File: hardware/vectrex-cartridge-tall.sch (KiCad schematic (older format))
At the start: 15 parts, among them CON1 vectrex-edge-connector, SW1 SW_DIP_x03, U1 AT27C256R-70PU / AT27C512R-70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, U2 DS2431+ TO-92

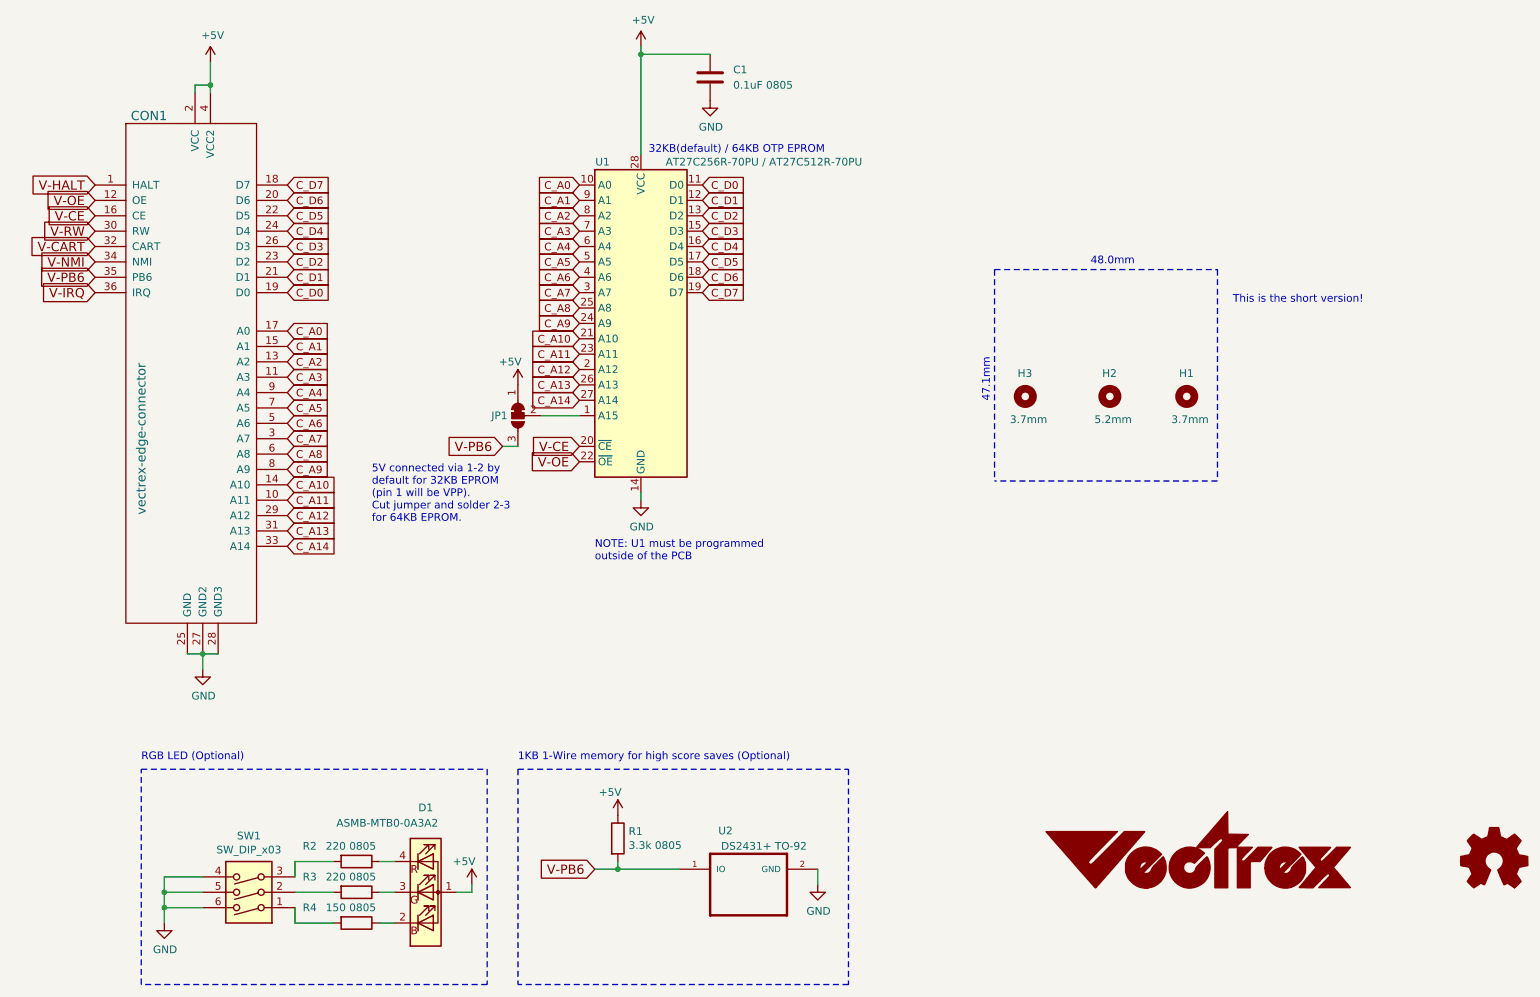
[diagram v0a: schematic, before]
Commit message: Updated DS2431 footprint, and many little tweaks for v1.2
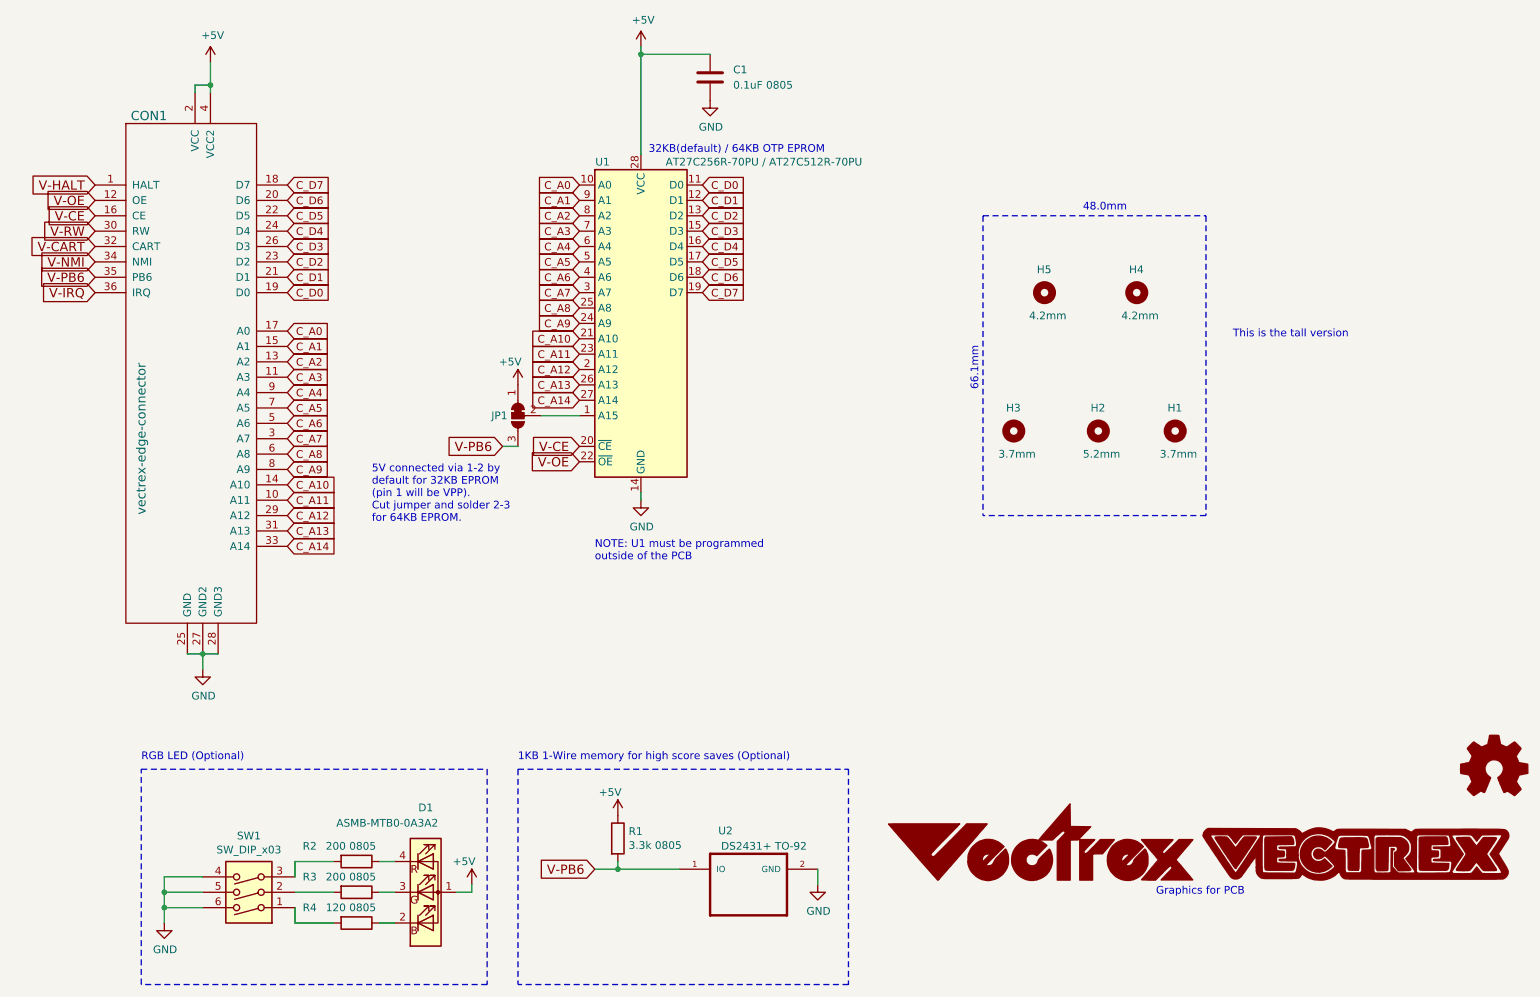
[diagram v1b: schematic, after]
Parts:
- added G3: LOGO, vectrex-cartridge:vectrex-uk-soldermask, symbol vectrex-uk:LOGO
- added H4, H5: 4.2mm, vectrex-cartridge:Mounting_Hole_D4.2mm, symbol Mechanical:MountingHole
- G1: footprint vectrex-cartridge:vectrex-us-soldermask-15mm -> vectrex-cartridge:vectrex-us-soldermask
- R2, R3: value 220 0805 -> 200 0805
- R4: value 150 0805 -> 120 0805
- U2: footprint vectrex-cartridge:TO-92L_HandSolder -> vectrex-cartridge:TO-92_Inline_BW
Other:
- note added: "66.1mm\n"
- note added: "Graphics for PCB"
- note added: "This is the tall version"
- note removed: "47.1mm\n"
- note removed: "This is the short version!"
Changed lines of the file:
@@
 Sheet 1 1
 Title "Vectrex Cartridge"
-Date "2020-06-28"
-Rev "v1.1"
+Date "2020-07-05"
+Rev "v1.2"
 Comp "Brett Walach"
 Comment1 ""
@@
 $Comp
 L vectrex-edge-connector:vectrex-edge-connector CON1
-U 1 1 59F1631A
+U 1 1 5F013EF4
 P 2550 3900
 F 0 "CON1" H 2200 5750 60  0000 C CNN
@@
 Connection ~ 2600 1850
 $Comp
-L Graphic:Logo_Open_Hardware_Small #LOGO1
-U 1 1 5EE7732D
-P 10950 6900
-F 0 "#LOGO1" H 10950 7175 50  0001 C CNN
-F 1 "Logo_Open_Hardware_Small" H 10950 6675 50  0001 C CNN
-F 2 "" H 10950 6900 50  0001 C CNN
-F 3 "~" H 10950 6900 50  0001 C CNN
-	1    10950 6900
-	1    0    0    -1
-$EndComp
-$Comp
 L power:+5V #PWR0101
-U 1 1 5EEE6CE5
+U 1 1 5F013EF6
 P 2600 1700
 F 0 "#PWR0101" H 2600 1550 50  0001 C CNN
@@
 $Comp
 L power:GND #PWR0102
-U 1 1 5EEFB74E
+U 1 1 5F013EFE
 P 2550 5650
 F 0 "#PWR0102" H 2550 5400 50  0001 C CNN
@@
 Wire Wire Line
 	2550 5550 2550 5650
-$Comp
-L Mechanical:MountingHole H1
-U 1 1 5EF10A41
-P 8950 3875
-F 0 "H1" H 8900 4025 50  0000 L CNN
-F 1 "3.7mm" H 8850 3725 50  0000 L CNN
-F 2 "vectrex-cartridge:Mounting_Hole_D3.7mm" H 8950 3875 50  0001 C CNN
-F 3 "~" H 8950 3875 50  0001 C CNN
-	1    8950 3875
-	1    0    0    -1
-$EndComp
-$Comp
-L Mechanical:MountingHole H3
-U 1 1 5EF12821
-P 7900 3875
-F 0 "H3" H 7850 4025 50  0000 L CNN
-F 1 "3.7mm" H 7800 3725 50  0000 L CNN
-F 2 "vectrex-cartridge:Mounting_Hole_D3.7mm" H 7900 3875 50  0001 C CNN
-F 3 "~" H 7900 3875 50  0001 C CNN
-	1    7900 3875
-	1    0    0    -1
-$EndComp
-$Comp
-L Mechanical:MountingHole H2
-U 1 1 5EF12D4B
-P 8450 3875
-F 0 "H2" H 8400 4025 50  0000 L CNN
-F 1 "5.2mm" H 8350 3725 50  0000 L CNN
-F 2 "vectrex-cartridge:Mounting_Hole_D5.2mm" H 8450 3875 50  0001 C CNN
-F 3 "~" H 8450 3875 50  0001 C CNN
-	1    8450 3875
-	1    0    0    -1
-$EndComp
-Wire Notes Line style solid
-	7700 3050 9150 3050
-Wire Notes Line style solid
-	9150 4425 7700 4425
-Wire Notes Line style solid
-	9150 3050 9150 4425
-Wire Notes Line style solid
-	7700 3050 7700 4425
-Text Notes 8325 3025 0    50   ~ 0
-48.0mm
-Text Notes 7675 3625 3    50   ~ 0
-47.1mm\n
 Text GLabel 5800 3200 2    50   Input ~ 0
 C_D7
@@
 $Comp
 L Device:R R1
-U 1 1 5EEF9998
+U 1 1 5F013EFC
 P 5250 6750
 F 0 "R1" H 5320 6796 50  0000 L CNN
@@
 $Comp
 L power:+5V #PWR0108
-U 1 1 5EEFA2B8
+U 1 1 5F013EFD
 P 5250 6600
 F 0 "#PWR0108" H 5250 6450 50  0001 C CNN
@@
 F 0 "U2" H 5950 7400 50  0000 C CNN
 F 1 "DS2431+ TO-92" H 6200 7300 50  0000 C CNN
-F 2 "vectrex-cartridge:TO-92L_HandSolder" H 5850 7050 50  0001 C CNN
+F 2 "vectrex-cartridge:TO-92_Inline_BW" H 5850 7050 50  0001 C CNN
 F 3 "" H 5850 7050 50  0001 C CNN
 	1    5850 7050
-	1    0    0    -1
-$EndComp
-$Comp
-L vectrex-us:LOGO G1
-U 1 1 5EF1F12E
-P 9025 6825
-F 0 "G1" H 9025 6605 60  0001 C CNN
-F 1 "LOGO" H 9025 7045 60  0001 C CNN
-F 2 "vectrex-cartridge:vectrex-us-soldermask-15mm" H 9025 6825 50  0001 C CNN
-F 3 "" H 9025 6825 50  0001 C CNN
-	1    9025 6825
 	1    0    0    -1
 $EndComp
@@
 P 3550 6900
 F 0 "R2" V 3450 6550 50  0000 L CNN
-F 1 "220 0805" V 3450 6700 50  0000 L CNN
+F 1 "200 0805" V 3450 6700 50  0000 L CNN
 F 2 "Resistor_SMD:R_0805_2012Metric_Pad1.15x1.40mm_HandSolder" V 3480 6900 50  0001 C CNN
 F 3 "~" H 3550 6900 50  0001 C CNN
@@
 P 3550 7100
 F 0 "R3" V 3450 6750 50  0000 L CNN
-F 1 "220 0805" V 3450 6900 50  0000 L CNN
+F 1 "200 0805" V 3450 6900 50  0000 L CNN
 F 2 "Resistor_SMD:R_0805_2012Metric_Pad1.15x1.40mm_HandSolder" V 3480 7100 50  0001 C CNN
 F 3 "~" H 3550 7100 50  0001 C CNN
@@
 P 3550 7300
 F 0 "R4" V 3450 6950 50  0000 L CNN
-F 1 "150 0805" V 3450 7100 50  0000 L CNN
+F 1 "120 0805" V 3450 7100 50  0000 L CNN
 F 2 "Resistor_SMD:R_0805_2012Metric_Pad1.15x1.40mm_HandSolder" V 3480 7300 50  0001 C CNN
 F 3 "~" H 3550 7300 50  0001 C CNN
@@
 Wire Wire Line
 	3150 7300 3400 7300
-Text Notes 9250 3275 0    50   ~ 0
-This is the short version!
+$Comp
+L Mechanical:MountingHole H3
+U 1 1 5F01A0BA
+P 7825 4100
+F 0 "H3" H 7775 4250 50  0000 L CNN
+F 1 "3.7mm" H 7725 3950 50  0000 L CNN
+F 2 "vectrex-cartridge:Mounting_Hole_D3.7mm" H 7825 4100 50  0001 C CNN
+F 3 "~" H 7825 4100 50  0001 C CNN
+	1    7825 4100
+	1    0    0    -1
+$EndComp
+$Comp
+L Mechanical:MountingHole H2
+U 1 1 5F01A0C0
+P 8375 4100
+F 0 "H2" H 8325 4250 50  0000 L CNN
+F 1 "5.2mm" H 8275 3950 50  0000 L CNN
+F 2 "vectrex-cartridge:Mounting_Hole_D5.2mm" H 8375 4100 50  0001 C CNN
+F 3 "~" H 8375 4100 50  0001 C CNN
+	1    8375 4100
+	1    0    0    -1
+$EndComp
+$Comp
+L Mechanical:MountingHole H5
+U 1 1 5F01A0C6
+P 8025 3200
+F 0 "H5" H 7975 3350 50  0000 L CNN
+F 1 "4.2mm" H 7925 3050 50  0000 L CNN
+F 2 "vectrex-cartridge:Mounting_Hole_D4.2mm" H 8025 3200 50  0001 C CNN
+F 3 "~" H 8025 3200 50  0001 C CNN
+	1    8025 3200
+	1    0    0    -1
+$EndComp
+$Comp
+L Mechanical:MountingHole H4
+U 1 1 5F01A0CC
+P 8625 3200
+F 0 "H4" H 8575 3350 50  0000 L CNN
+F 1 "4.2mm" H 8525 3050 50  0000 L CNN
+F 2 "vectrex-cartridge:Mounting_Hole_D4.2mm" H 8625 3200 50  0001 C CNN
+F 3 "~" H 8625 3200 50  0001 C CNN
+	1    8625 3200
+	1    0    0    -1
+$EndComp
+Wire Notes Line style solid
+	7625 2700 9075 2700
+Wire Notes Line style solid
+	9075 4650 7625 4650
+Wire Notes Line style solid
+	9075 2700 9075 4650
+Wire Notes Line style solid
+	7625 2700 7625 4650
+Text Notes 8275 2675 0    50   ~ 0
+48.0mm
+Text Notes 7600 3550 3    50   ~ 0
+66.1mm\n
+Text Notes 9250 3500 0    50   ~ 0
+This is the tall version
+$Comp
+L Graphic:Logo_Open_Hardware_Small #LOGO1
+U 1 1 5F021A94
+P 10950 6300
+F 0 "#LOGO1" H 10950 6575 50  0001 C CNN
+F 1 "Logo_Open_Hardware_Small" H 10950 6075 50  0001 C CNN
+F 2 "" H 10950 6300 50  0001 C CNN
+F 3 "~" H 10950 6300 50  0001 C CNN
+	1    10950 6300
+	1    0    0    -1
+$EndComp
+Text Notes 8750 7125 0    50   ~ 0
+Graphics for PCB
+$Comp
+L vectrex-uk:LOGO G3
+U 1 1 5F021AA1
+P 10050 6850
+F 0 "G3" H 10050 6710 60  0001 C CNN
+F 1 "LOGO" H 10050 6990 60  0001 C CNN
+F 2 "vectrex-cartridge:vectrex-uk-soldermask" H 10050 6850 50  0001 C CNN
+F 3 "" H 10050 6850 50  0001 C CNN
+	1    10050 6850
+	1    0    0    -1
+$EndComp
+$Comp
+L vectrex-us:LOGO G1
+U 1 1 5F021AA7
+P 8000 6775
+F 0 "G1" H 8000 6555 60  0001 C CNN
+F 1 "LOGO" H 8000 6995 60  0001 C CNN
+F 2 "vectrex-cartridge:vectrex-us-soldermask" H 8000 6775 50  0001 C CNN
+F 3 "" H 8000 6775 50  0001 C CNN
+	1    8000 6775
+	1    0    0    -1
+$EndComp
+$Comp
+L Mechanical:MountingHole H1
+U 1 1 5F01A0B4
+P 8875 4100
+F 0 "H1" H 8825 4250 50  0000 L CNN
+F 1 "3.7mm" H 8775 3950 50  0000 L CNN
+F 2 "vectrex-cartridge:Mounting_Hole_D3.7mm" H 8875 4100 50  0001 C CNN
+F 3 "~" H 8875 4100 50  0001 C CNN
+	1    8875 4100
+	1    0    0    -1
+$EndComp
 $EndSCHEMATC
